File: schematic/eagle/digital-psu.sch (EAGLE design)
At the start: 79 parts, among them IC1 TL072P, IC2 TLC272P, Q1 MPSA56-TO92, T3 2N3055, T4 2N3055, T5 2N3055, X1 Vout, X2 PASS_TRANSISTORS, X3 AC_IN

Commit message: fixed a few small errors
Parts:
- R27: value 10k -> 100
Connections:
- new net N$32: R11.1, R12/1.A, R12/2.A
- net N$20: no longer R11.1, R12/1.A, R12/2.A
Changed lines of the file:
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@@
 <part name="C2" library="resistor" deviceset="CPOL-EU" device="E10-22.5" value="10mF"/>
 <part name="C3" library="resistor" deviceset="CPOL-EU" device="E10-22.5" value="10mF"/>
-<part name="R27" library="rcl" deviceset="R-TRIMM" device="64W" value="10k"/>
+<part name="R27" library="rcl" deviceset="R-TRIMM" device="64W" value="100"/>
 <part name="SUPPLY18" library="supply2" deviceset="GND" device=""/>
 <part name="T2" library="transistor" deviceset="*-NPN-" device="TO92-EBC"/>
@@
 <net name="N$20" class="0">
 <segment>
-<pinref part="R12" gate="/1" pin="A"/>
-<pinref part="R12" gate="/2" pin="A"/>
-<wire x1="213.36" y1="254" x2="198.12" y2="254" width="0.1524" layer="91"/>
-<pinref part="R11" gate="G$1" pin="1"/>
 <wire x1="172.72" y1="241.3" x2="190.5" y2="241.3" width="0.1524" layer="91"/>
-<wire x1="190.5" y1="243.84" x2="190.5" y2="254" width="0.1524" layer="91"/>
-<wire x1="190.5" y1="254" x2="185.42" y2="254" width="0.1524" layer="91"/>
 <pinref part="C13" gate="G$1" pin="2"/>
-<wire x1="198.12" y1="254" x2="190.5" y2="254" width="0.1524" layer="91"/>
-<junction x="198.12" y="254"/>
-<junction x="190.5" y="254"/>
 <wire x1="190.5" y1="241.3" x2="190.5" y2="243.84" width="0.1524" layer="91"/>
 <pinref part="R12" gate="/1" pin="E"/>
@@
 <junction x="198.12" y="243.84"/>
 <wire x1="190.5" y1="243.84" x2="198.12" y2="243.84" width="0.1524" layer="91"/>
-<junction x="190.5" y="243.84"/>
 <pinref part="IC1" gate="B" pin="-IN"/>
 <wire x1="154.94" y1="251.46" x2="154.94" y2="241.3" width="0.1524" layer="91"/>
-<wire x1="154.94" y1="241.3" x2="170.18" y2="241.3" width="0.1524" layer="91"/>
-<wire x1="170.18" y1="241.3" x2="172.72" y2="241.3" width="0.1524" layer="91"/>
+<wire x1="154.94" y1="241.3" x2="172.72" y2="241.3" width="0.1524" layer="91"/>
 <junction x="172.72" y="241.3"/>
 </segment>
 </net>
-<net name="N$23" class="0">
+<net name="N$40" class="0">
 <segment>
 <pinref part="R11" gate="G$1" pin="2"/>
@@
 </segment>
 </net>
+<net name="N$32" class="0">
+<segment>
+<pinref part="R11" gate="G$1" pin="1"/>
+<pinref part="R12" gate="/1" pin="A"/>
+<pinref part="R12" gate="/2" pin="A"/>
+<wire x1="213.36" y1="254" x2="198.12" y2="254" width="0.1524" layer="91"/>
+<junction x="198.12" y="254"/>
+<wire x1="198.12" y1="254" x2="185.42" y2="254" width="0.1524" layer="91"/>
+</segment>
+</net>

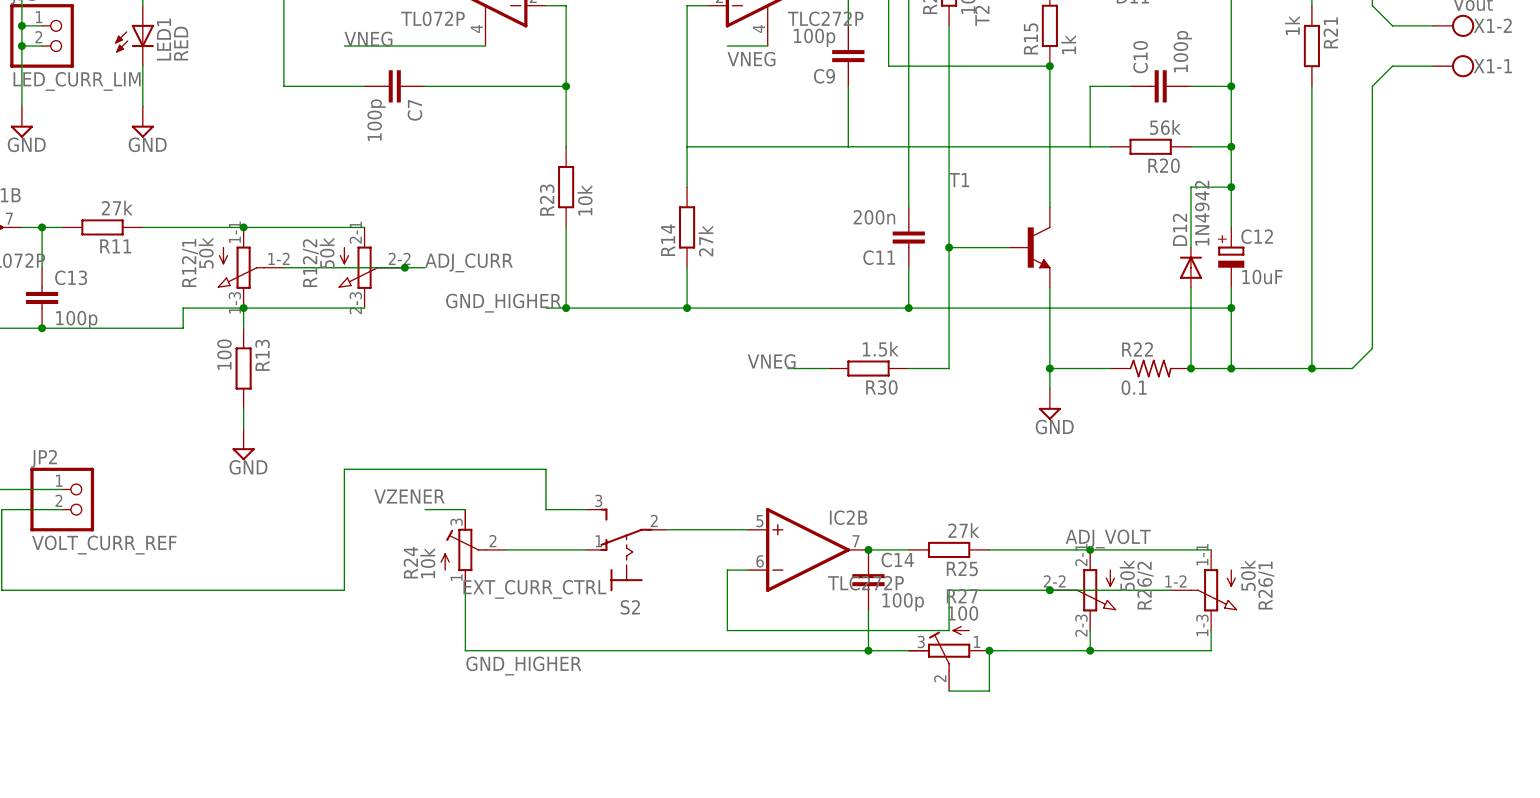
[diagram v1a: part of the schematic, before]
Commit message: fixed op amp output errors
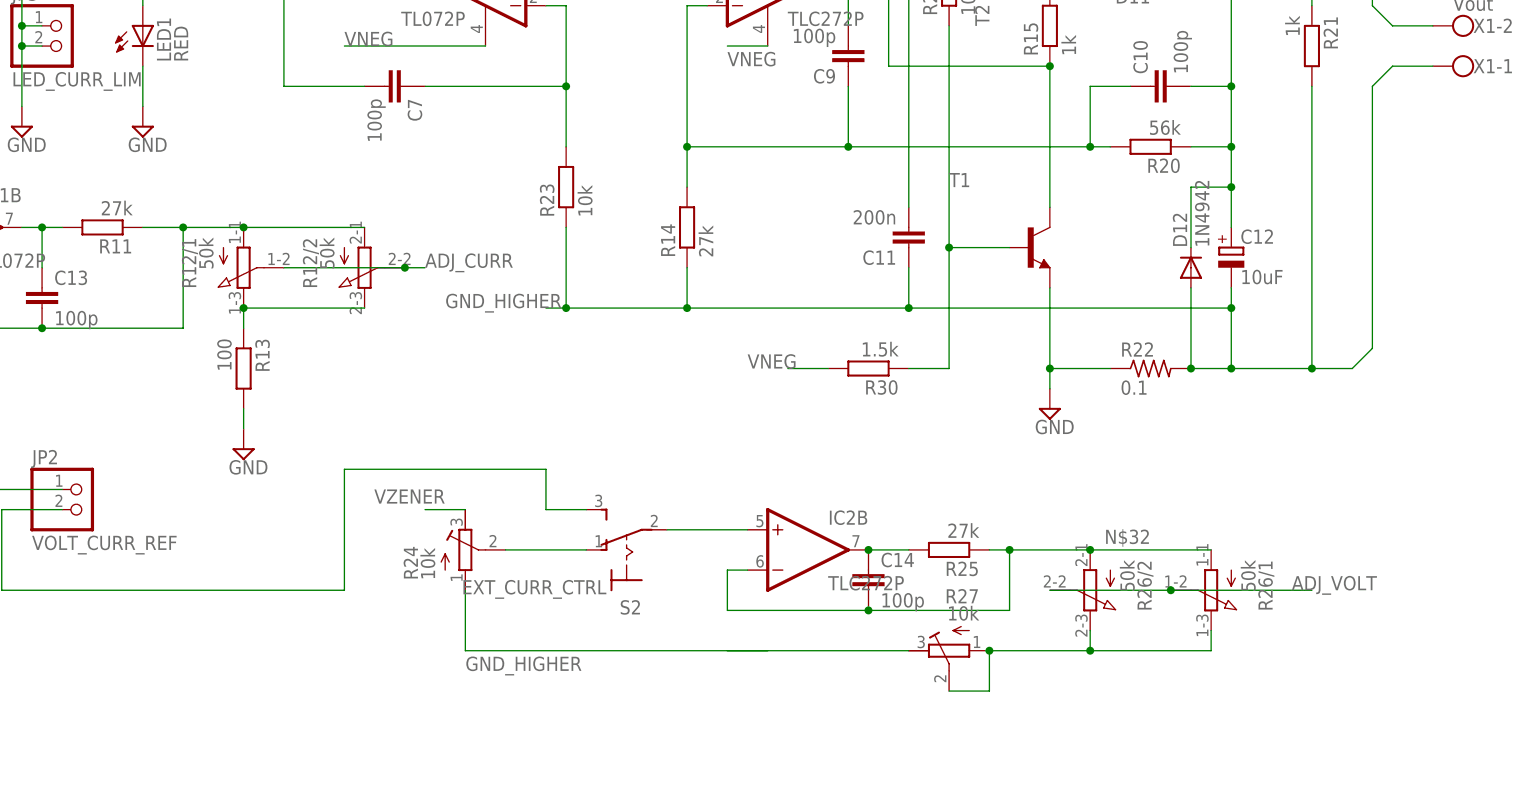
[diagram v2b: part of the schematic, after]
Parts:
- R27: value 100 -> 10k
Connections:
- net ADJ_VOLT: now also R26/1.S, R26/2.S; no longer R25.1, R26/1.A, R26/2.A
- net GND_HIGHER: no longer C14.2
- net N$2: now also R12/1.E, R12/2.E, R13.1; no longer IC2B.-IN, R26/1.S, R26/2.S
- net N$20: now also R11.1, R12/1.A, R12/2.A; no longer R12/1.E, R12/2.E, R13.1
- net N$32: now also C14.2, IC2B.-IN, R25.1, R26/1.A, R26/2.A; no longer R11.1, R12/1.A, R12/2.A
